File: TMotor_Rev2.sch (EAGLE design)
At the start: 29 parts, among them U1 INA125U, U2 INA125U

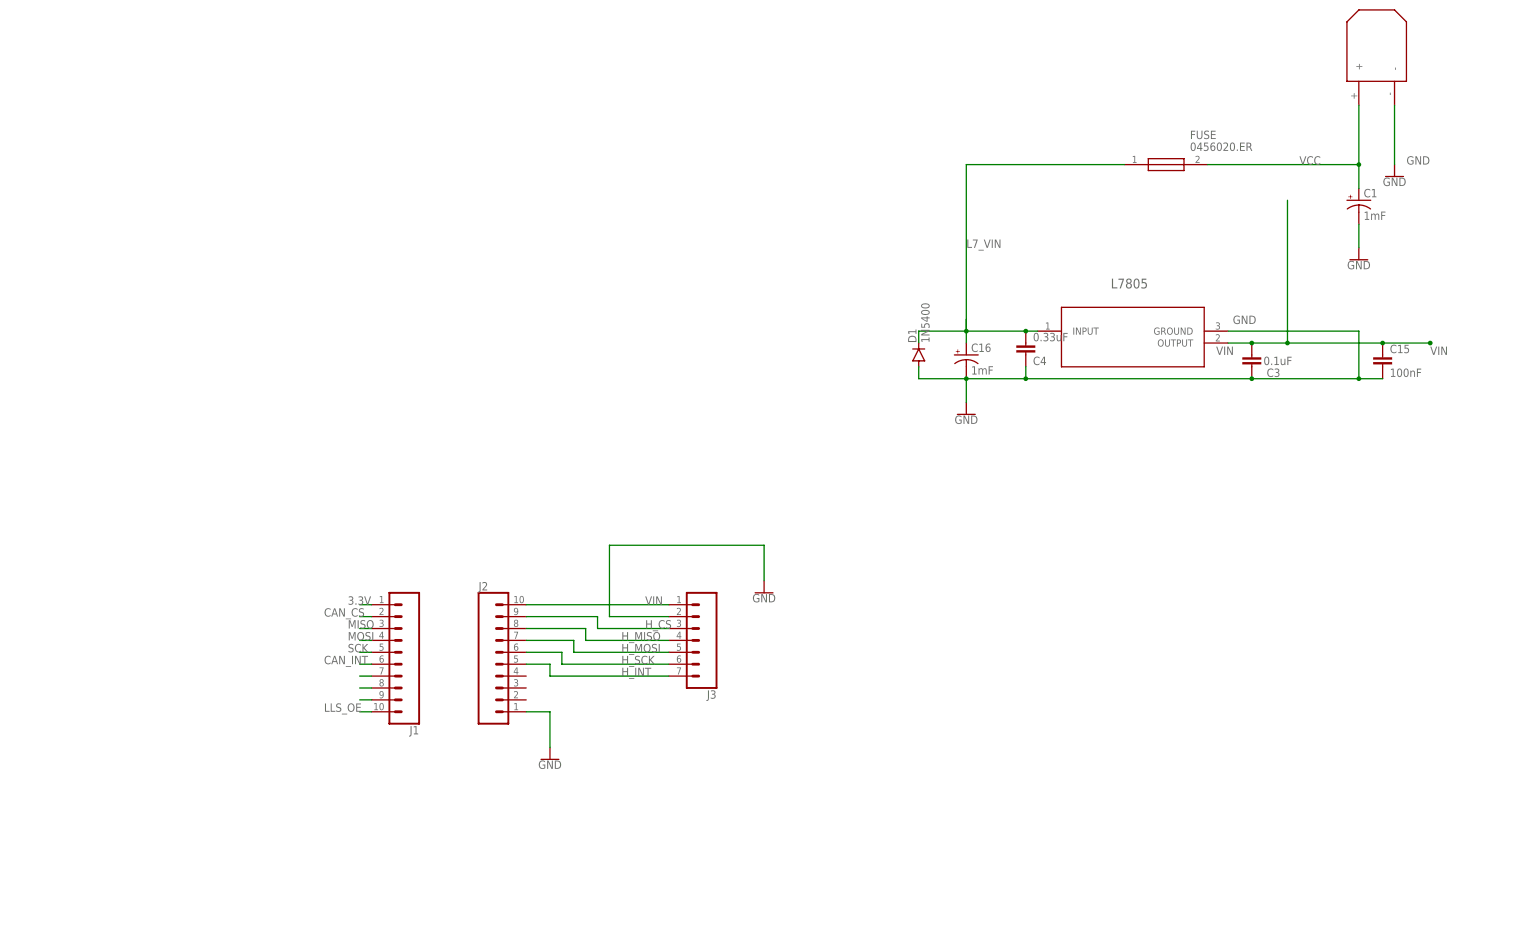
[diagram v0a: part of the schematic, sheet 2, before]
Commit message: Added integrated PCB version w/ MCP25625
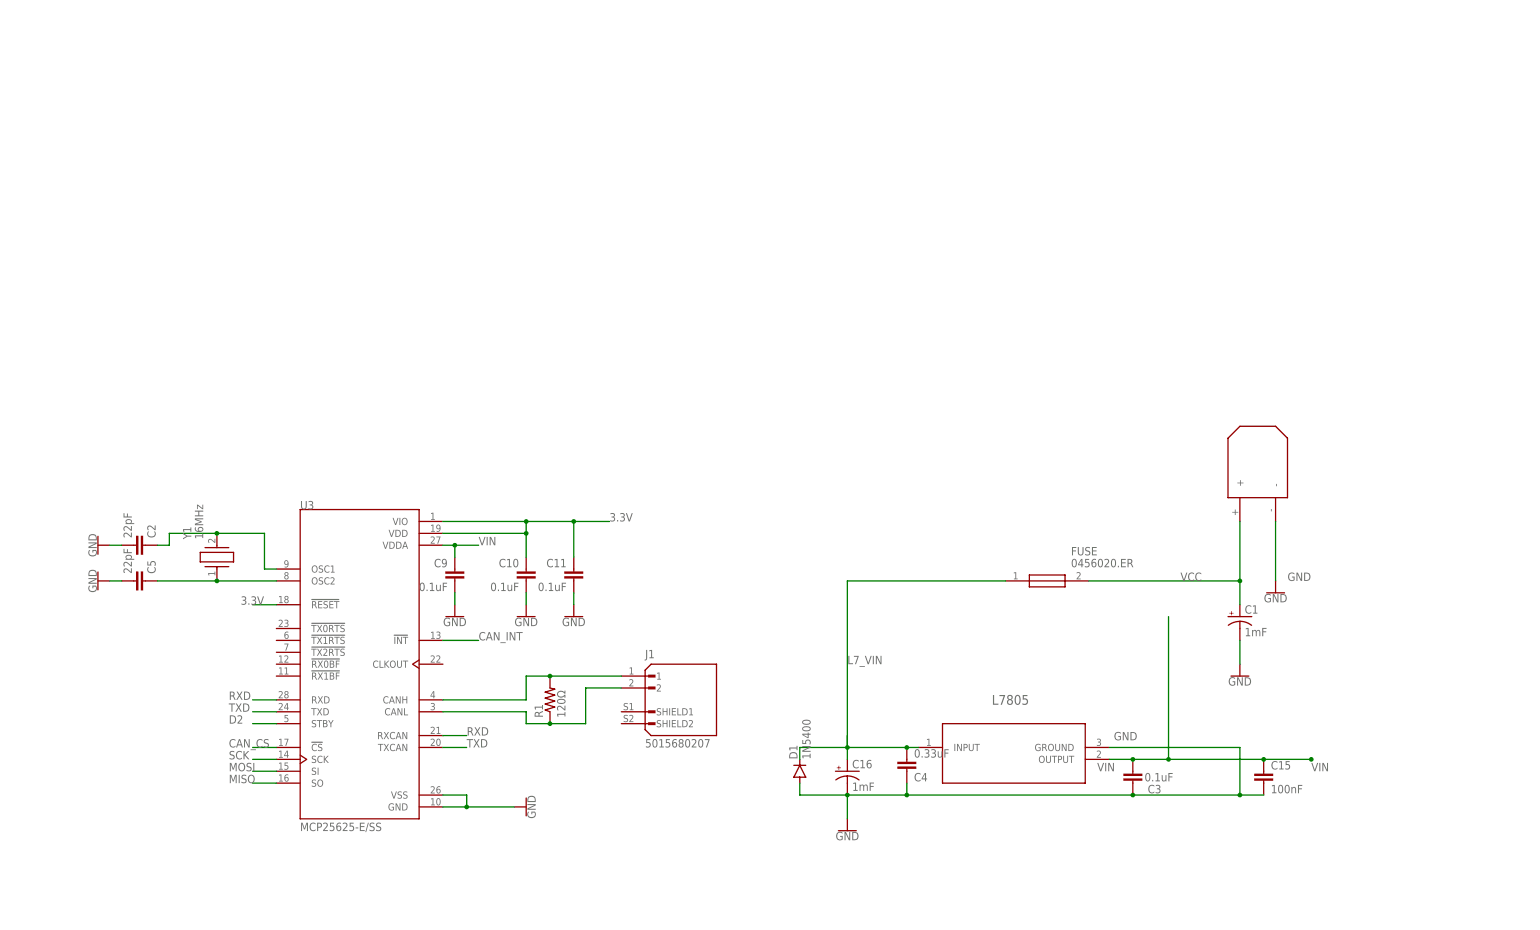
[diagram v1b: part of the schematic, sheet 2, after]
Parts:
- removed J2: (no value), SparkFun-Connectors:CONN_10"
- removed J3: (no value), SparkFun-Connectors:CONN_07
- added C10, C11, C9: 0.1uF, rcl:C-EU050-024X044
- added C2, C5: 22pF, rcl:C-EU050-024X044
- added R1: 120Ω, rcl:R-US_0207/10
- added U3: MCP25625-E/SS, MCP25625-E_SS:MCP25625-E/SS
- added Y1: 16MHz, SnapEDA-Library_Paul:4.91520MHZ_HC49_4H_30_50_-40+8
- J1: value (none) -> 5015680207; device SparkFun-Connectors:CONN_10" -> SnapEDA-Library_Paul:5015680207
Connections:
- removed net H_CS: J2.9, J3.3
- removed net H_INT: J2.5, J3.7
- removed net H_MISO: J2.8, J3.4
- removed net H_MOSI: J2.7, J3.5
- removed net H_SCK: J2.6, J3.6
- removed net N$27: J1.7
- removed net N$28: J1.8
- removed net N$29: J1.9
- new net CANH-: J1.1, R1.2, U3.CANH
- new net CANL-: J1.2, R1.1, U3.CANL
- new net D2: U3.STBY, USB.D2
- new net N$1: C2.1, U3.OSC1, Y1.2
- new net N$2: C5.1, U3.OSC2, Y1.1
- new net RXD: U3.RXCAN, U3.RXD
- new net TXD: U3.TXCAN, U3.TXD
- net 3.3V: now also C10.1, C11.1, U3.!RESET, U3.VDD, U3.VIO; no longer J1.1
- net CAN_CS: now also U3.!CS; no longer J1.2
- net CAN_INT: now also U3.!INT; no longer J1.6
- net GND: now also C10.2, C11.2, C2.2, C5.2, C9.2, U3.GND, U3.VSS; no longer J2.1, J3.2
- net LLS_OE: no longer J1.10
- net MISO: now also U3.SO; no longer J1.3
- net MOSI: now also U3.SI; no longer J1.4
- net SCK: now also U3.SCK; no longer J1.5
- net VIN: now also C9.1, U3.VDDA; no longer J2.10, J3.1
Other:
- moved on the sheet: C1, C15, C16, C3, C4, D1, FUSE, L7805
